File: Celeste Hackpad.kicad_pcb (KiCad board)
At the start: 2 copper layers, 159.5 x 45.2 mm, 29 parts, among them J1 OLED, SW9 EC11, U1 XIAO-RP2040-SMD

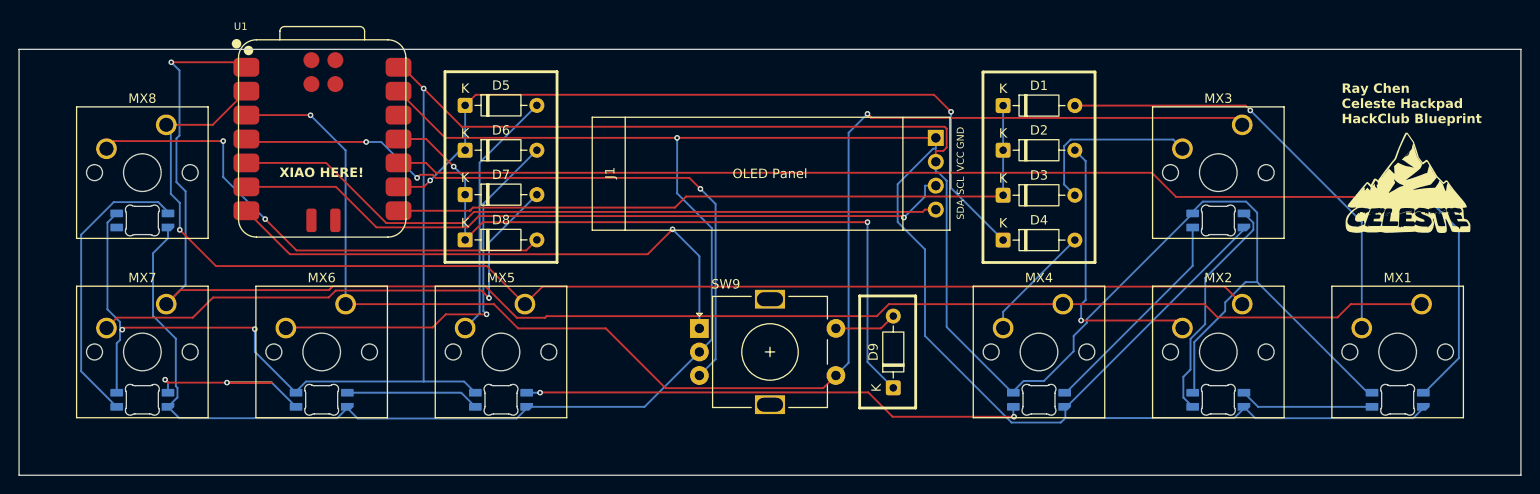
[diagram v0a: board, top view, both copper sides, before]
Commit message: Redraw tracks by hand
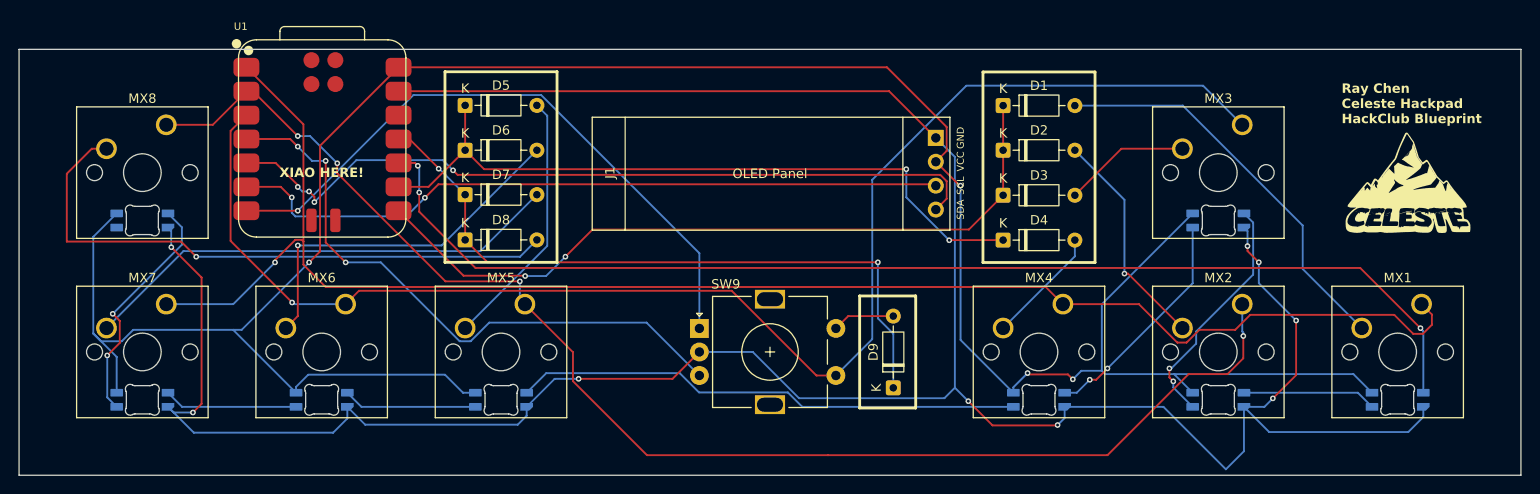
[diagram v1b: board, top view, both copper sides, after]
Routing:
- net Net-(LED6-DOUT): track 37.4 -> 14.2 mm, vias 2 -> 0
- net GND: track 277.1 -> 293.5 mm, vias 1 -> 9
- net Net-(D8-A): track 53.6 -> 63.9 mm, vias 2 -> 1
- net led: track 134.6 -> 125.6 mm, vias 1 -> 3
- net EC11A: track 60.0 -> 68.2 mm
- net EC11B: track 71.9 -> 65.2 mm
- net row2: track 82.9 -> 76.3 mm
- net SDA: track 76.5 -> 82.8 mm, vias 0 -> 4
- net col2: track 139.4 -> 145.5 mm, vias 1 -> 4
- net Net-(D2-A): track 29.9 -> 23.8 mm
- net Net-(LED7-DOUT): track 31.1 -> 25.5 mm, vias 0 -> 2
- net row1: track 74.6 -> 80.2 mm, vias 0 -> 2
- net Net-(D3-A): track 19.0 -> 13.5 mm
- net row3: track 77.6 -> 73.2 mm
- net Net-(D7-A): track 55.7 -> 51.6 mm, vias 1 -> 0
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
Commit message: Shrink size of pcb
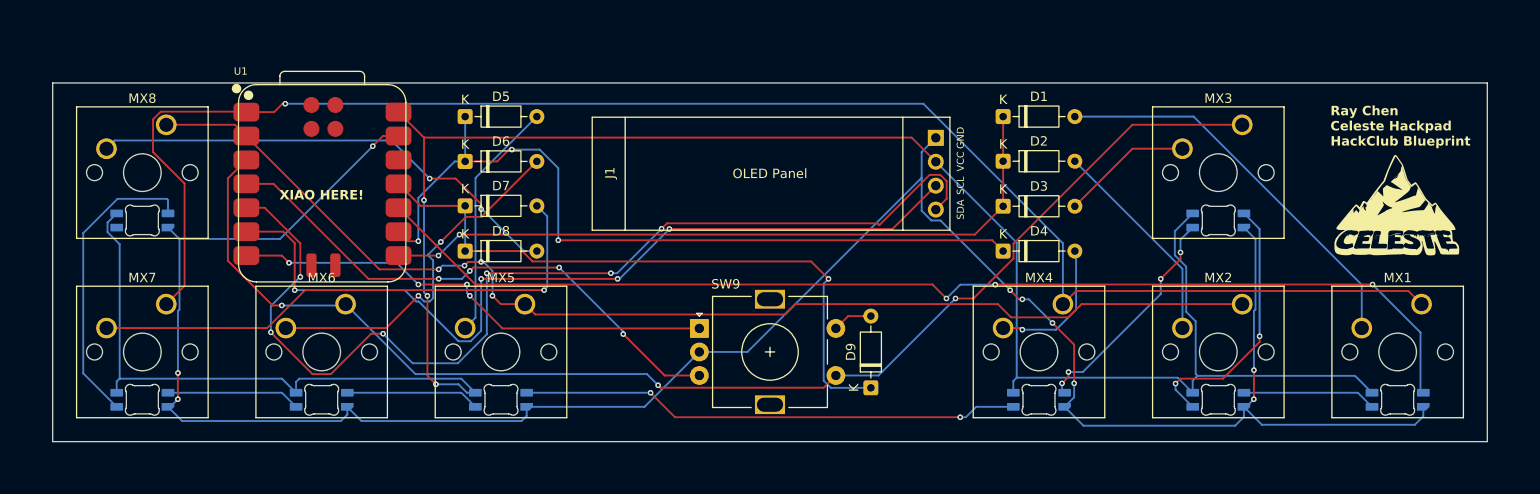
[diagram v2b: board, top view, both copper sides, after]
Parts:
- moved U1 4.76 mm to (67.9, 50.0)
- moved G*** 2.66 mm to (182.2, 52.4)
- moved D9 2.38 mm to (126.2, 71.7)
- moved D6 1.19 mm to (83.1, 47.6)
- moved D5 1.19 mm to (83.1, 42.9)
- moved D7 1.19 mm to (83.1, 52.3)
- moved D8 1.19 mm to (83.1, 57.1)
- moved D2 1.17 mm to (140.3, 47.6)
- moved D3 1.17 mm to (140.3, 52.4)
- moved D4 1.17 mm to (140.3, 57.1)
- moved D1 1.17 mm to (140.3, 42.9)
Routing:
- net GND: track 293.5 -> 241.9 mm
- net SDA: track 82.8 -> 110.8 mm, vias 4 -> 6
- net VCC: track 260.4 -> 238.9 mm, vias 4 -> 3
- net col2: track 145.5 -> 126.5 mm
- net EC11A: track 68.2 -> 51.9 mm, vias 1 -> 4
- net EC11SWB: track 153.0 -> 137.5 mm, vias 1 -> 3
- net SCL: track 77.0 -> 91.1 mm, vias 2 -> 4
- net Net-(D8-A): track 63.9 -> 51.3 mm, vias 1 -> 2
- net row2: track 76.3 -> 85.1 mm, vias 2 -> 3
- net EC11B: track 65.2 -> 57.7 mm, vias 3 -> 4
- net Net-(LED7-DOUT): track 25.5 -> 31.9 mm, vias 2 -> 0
- net Net-(D7-A): track 51.6 -> 57.7 mm, vias 0 -> 1
- net row1: track 80.2 -> 75.9 mm
- net row3: track 73.2 -> 69.0 mm, vias 2 -> 1
- net led: track 125.6 -> 121.8 mm
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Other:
- board size 159.5 x 45.2 mm -> 152.4 x 38.1 mm
